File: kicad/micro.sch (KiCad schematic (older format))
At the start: 5 parts

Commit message: hardware prototype for v2.0 board
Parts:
- added P11: SERIAL, symbol CONN_3
- added R3: 1k, ~, symbol R
- added SW2: MODE SW, ~, symbol SWITCH_INV
- gave numbers to parts that had none: 5
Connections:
- net +5V: now also R3.1
- net GND: now also P11.3 (P3), SW2.1
- net RX: now reaches IC1.2 ((PCINT8/RXD0)PE0)
- net RX: now also P11.1 (P1)
- net TX: now reaches IC1.3 ((TXD0)PE1)
- net TX: now also P11.2 (PM)
- net A_FCMD_I: now reaches IC1.7 ((OC3C/INT5)PE5)
- net MODE: now reaches IC1.8 ((T3/INT6)PE6)
- net MODE: now also R3.2, SW2.2
- net A_ETHINT: no longer names the net of IC1.5 ((OC3A/AIN1)PE3)
- net A_FDCINT renamed A_FCFG_I
- net C_~RESET renamed ~RESET
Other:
- moved on the sheet: C11, C12, R1, X1
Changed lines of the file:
@@
 $Descr USLegal 14000 8500
 encoding utf-8
-Sheet 3 4
+Sheet 3 3
 Title "Color Computer FDC Ethernet Controller"
-Date "31 jul 2013"
+Date "4 aug 2013"
 Rev "2.0"
 Comp "Bexkat Systems LLC 2013"
@@
 $EndDescr
 $Comp
-L ATMEGA2560-A IC?
+L ATMEGA2560-A IC1
 U 1 1 51D5E753
 P 6550 4200
-F 0 "IC?" H 5400 7000 40  0000 L BNN
+F 0 "IC1" H 5400 7000 40  0000 L BNN
 F 1 "ATMEGA2560-A" H 7250 1350 40  0000 L BNN
 F 2 "TQFP100" H 6550 4200 30  0000 C CIN
@@
 Text HLabel 5050 6300 0    60   Output ~ 0
 A_~SELECT
-Text HLabel 5000 1600 0    60   Input ~ 0
-C_~RESET
-Text HLabel 8100 5500 2    60   Input ~ 0
-A_ETHINT
+Text HLabel 5250 1600 0    60   Input ~ 0
+~RESET
 Text HLabel 8100 5600 2    60   Input ~ 0
-A_FDCINT
-$Comp
-L +5V #PWR?
+A_FCFG_I
+$Comp
+L +5V #PWR043
 U 1 1 51D60C51
 P 6500 1200
-F 0 "#PWR?" H 6500 1290 20  0001 C CNN
+F 0 "#PWR043" H 6500 1290 20  0001 C CNN
 F 1 "+5V" H 6500 1290 30  0000 C CNN
 F 2 "" H 6500 1200 60  0000 C CNN
@@
 Connection ~ 6500 1300
 $Comp
-L GND #PWR?
+L GND #PWR044
 U 1 1 51D60C7D
 P 6550 7200
-F 0 "#PWR?" H 6550 7200 30  0001 C CNN
+F 0 "#PWR044" H 6550 7200 30  0001 C CNN
 F 1 "GND" H 6550 7130 30  0001 C CNN
 F 2 "" H 6550 7200 60  0000 C CNN
@@
 Connection ~ 6550 7100
 $Comp
-L CRYSTAL X?
+L CRYSTAL X1
 U 1 1 51D60CD1
-P 3550 2000
-F 0 "X?" H 3550 2150 60  0000 C CNN
-F 1 "16MHz" H 3550 1850 60  0000 C CNN
-F 2 "~" H 3550 2000 60  0000 C CNN
-F 3 "~" H 3550 2000 60  0000 C CNN
-	1    3550 2000
-	1    0    0    -1
-$EndComp
-$Comp
-L R R?
+P 1800 1400
+F 0 "X1" H 1800 1550 60  0000 C CNN
+F 1 "16MHz" H 1800 1250 60  0000 C CNN
+F 2 "~" H 1800 1400 60  0000 C CNN
+F 3 "~" H 1800 1400 60  0000 C CNN
+	1    1800 1400
+	1    0    0    -1
+$EndComp
+$Comp
+L R R1
 U 1 1 51D60CE0
-P 3550 1700
-F 0 "R?" V 3630 1700 40  0000 C CNN
-F 1 "1M" V 3557 1701 40  0000 C CNN
-F 2 "~" V 3480 1700 30  0000 C CNN
-F 3 "~" H 3550 1700 30  0000 C CNN
-	1    3550 1700
+P 1800 1100
+F 0 "R1" V 1880 1100 40  0000 C CNN
+F 1 "1M" V 1807 1101 40  0000 C CNN
+F 2 "~" V 1730 1100 30  0000 C CNN
+F 3 "~" H 1800 1100 30  0000 C CNN
+	1    1800 1100
 	0    -1   -1   0
 $EndComp
 $Comp
-L C C?
+L C C11
 U 1 1 51D60D15
-P 3250 2300
-F 0 "C?" H 3250 2400 40  0000 L CNN
-F 1 "22pF" H 3256 2215 40  0000 L CNN
-F 2 "~" H 3288 2150 30  0000 C CNN
-F 3 "~" H 3250 2300 60  0000 C CNN
-	1    3250 2300
-	1    0    0    -1
-$EndComp
-$Comp
-L C C?
+P 1500 1700
+F 0 "C11" H 1500 1800 40  0000 L CNN
+F 1 "22pF" H 1506 1615 40  0000 L CNN
+F 2 "~" H 1538 1550 30  0000 C CNN
+F 3 "~" H 1500 1700 60  0000 C CNN
+	1    1500 1700
+	1    0    0    -1
+$EndComp
+$Comp
+L C C12
 U 1 1 51D60D24
-P 3850 2300
-F 0 "C?" H 3850 2400 40  0000 L CNN
-F 1 "22pF" H 3856 2215 40  0000 L CNN
-F 2 "~" H 3888 2150 30  0000 C CNN
-F 3 "~" H 3850 2300 60  0000 C CNN
-	1    3850 2300
-	1    0    0    -1
-$EndComp
-Connection ~ 3850 2000
-Connection ~ 3250 2000
-Wire Wire Line
-	3250 2500 3850 2500
-$Comp
-L GND #PWR?
+P 2100 1700
+F 0 "C12" H 2100 1800 40  0000 L CNN
+F 1 "22pF" H 2106 1615 40  0000 L CNN
+F 2 "~" H 2138 1550 30  0000 C CNN
+F 3 "~" H 2100 1700 60  0000 C CNN
+	1    2100 1700
+	1    0    0    -1
+$EndComp
+Connection ~ 2100 1400
+Connection ~ 1500 1400
+Wire Wire Line
+	1500 1900 2100 1900
+$Comp
+L GND #PWR045
 U 1 1 51D60D76
-P 3550 2550
-F 0 "#PWR?" H 3550 2550 30  0001 C CNN
-F 1 "GND" H 3550 2480 30  0001 C CNN
-F 2 "" H 3550 2550 60  0000 C CNN
-F 3 "" H 3550 2550 60  0000 C CNN
-	1    3550 2550
-	1    0    0    -1
-$EndComp
-Wire Wire Line
-	3550 2500 3550 2550
-Connection ~ 3550 2500
-Wire Wire Line
-	3800 1700 3850 1700
-Wire Wire Line
-	3850 1700 3850 2100
-Wire Wire Line
-	3250 2100 3250 1700
-Wire Wire Line
-	3250 1700 3300 1700
-Text Label 3850 2000 0    60   ~ 0
+P 1800 1950
+F 0 "#PWR045" H 1800 1950 30  0001 C CNN
+F 1 "GND" H 1800 1880 30  0001 C CNN
+F 2 "" H 1800 1950 60  0000 C CNN
+F 3 "" H 1800 1950 60  0000 C CNN
+	1    1800 1950
+	1    0    0    -1
+$EndComp
+Wire Wire Line
+	1800 1900 1800 1950
+Connection ~ 1800 1900
+Wire Wire Line
+	2050 1100 2100 1100
+Wire Wire Line
+	2100 1100 2100 1500
+Wire Wire Line
+	1500 1500 1500 1100
+Wire Wire Line
+	1500 1100 1550 1100
+Text Label 2100 1400 0    60   ~ 0
 XTAL2
-Text Label 3250 2000 2    60   ~ 0
+Text Label 1500 1400 2    60   ~ 0
 XTAL1
 Text Label 5250 2200 2    60   ~ 0
@@
 	7850 2300 8050 2300
 Wire Wire Line
-	7850 5500 8100 5500
-Wire Wire Line
 	7850 5600 8100 5600
 Wire Wire Line
@@
 Wire Wire Line
 	5000 3200 5250 3200
-Wire Wire Line
-	5000 1600 5250 1600
+$Comp
+L CONN_3 P11
+U 1 1 51FB918E
+P 9350 5300
+F 0 "P11" V 9300 5300 50  0000 C CNN
+F 1 "SERIAL" V 9400 5300 40  0000 C CNN
+F 2 "" H 9350 5300 60  0000 C CNN
+F 3 "" H 9350 5300 60  0000 C CNN
+	1    9350 5300
+	1    0    0    -1
+$EndComp
+Wire Wire Line
+	7850 5200 9000 5200
+Wire Wire Line
+	7850 5300 9000 5300
+$Comp
+L GND #PWR046
+U 1 1 51FB9229
+P 8950 5500
+F 0 "#PWR046" H 8950 5500 30  0001 C CNN
+F 1 "GND" H 8950 5430 30  0001 C CNN
+F 2 "" H 8950 5500 60  0000 C CNN
+F 3 "" H 8950 5500 60  0000 C CNN
+	1    8950 5500
+	1    0    0    -1
+$EndComp
+Wire Wire Line
+	8950 5500 8950 5400
+Wire Wire Line
+	8950 5400 9000 5400
+$Comp
+L SWITCH_INV SW2
+U 1 1 51FC2D05
+P 10500 5800
+F 0 "SW2" H 10300 5950 50  0000 C CNN
+F 1 "MODE SW" H 10350 5650 50  0000 C CNN
+F 2 "~" H 10500 5800 60  0000 C CNN
+F 3 "~" H 10500 5800 60  0000 C CNN
+	1    10500 5800
+	1    0    0    -1
+$EndComp
+Text HLabel 8100 5700 2    60   Input ~ 0
+A_FCMD_I
+Wire Wire Line
+	7850 5700 8100 5700
+$Comp
+L +5V #PWR047
+U 1 1 51FC56B4
+P 9750 5200
+F 0 "#PWR047" H 9750 5290 20  0001 C CNN
+F 1 "+5V" H 9750 5290 30  0000 C CNN
+F 2 "" H 9750 5200 60  0000 C CNN
+F 3 "" H 9750 5200 60  0000 C CNN
+	1    9750 5200
+	1    0    0    -1
+$EndComp
+$Comp
+L R R3
+U 1 1 51FC56DA
+P 9750 5550
+F 0 "R3" V 9830 5550 40  0000 C CNN
+F 1 "1k" V 9757 5551 40  0000 C CNN
+F 2 "~" V 9680 5550 30  0000 C CNN
+F 3 "~" H 9750 5550 30  0000 C CNN
+	1    9750 5550
+	1    0    0    -1
+$EndComp
+Wire Wire Line
+	9750 5200 9750 5300
+Wire Wire Line
+	7850 5800 10000 5800
+Connection ~ 9750 5800
+$Comp
+L GND #PWR048
+U 1 1 51FC57B8
+P 11100 6000
+F 0 "#PWR048" H 11100 6000 30  0001 C CNN
+F 1 "GND" H 11100 5930 30  0001 C CNN
+F 2 "" H 11100 6000 60  0000 C CNN
+F 3 "" H 11100 6000 60  0000 C CNN
+	1    11100 6000
+	1    0    0    -1
+$EndComp
+Text Label 8850 5800 0    60   ~ 0
+MODE
+Text Label 7850 5200 0    60   ~ 0
+RX
+Text Label 7850 5300 0    60   ~ 0
+TX
+Wire Wire Line
+	11000 5700 11100 5700
+Wire Wire Line
+	11100 5700 11100 6000
 $EndSCHEMATC

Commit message: start of additional goodness and fixes
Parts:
- removed R3: 1k, ~, symbol R
- added D10: A0, symbol LED
- added D11: A1, symbol LED
- added D12: A2, symbol LED
- added D13: A3, symbol LED
- added RP2: 150, symbol R_PACK4
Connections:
- net GND: now also D10.2 (K), D11.2 (K), D12.2 (K), D13.2 (K)
- net LED0: now reaches IC1.15 (PH3(OC4A))
- net LED0: now also RP2.1 (P1)
- net LED1: now reaches IC1.16 (PH4(OC4B))
- net LED1: now also RP2.2 (P2)
- net LED2: now reaches IC1.17 (PH5(OC4C))
- net LED2: now also RP2.3 (P3)
- net LED3: now reaches IC1.18 (PH6(OC2B))
- net LED3: now also RP2.4 (P4)
- new net: D13.1 (A), RP2.5 (R4)
- new net: D11.1 (A), RP2.7 (R2)
- new net: D10.1 (A), RP2.8 (R1)
- new net: D12.1 (A), RP2.6 (R3)
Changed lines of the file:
@@
 Sheet 3 3
 Title "Color Computer FDC Ethernet Controller"
-Date "4 aug 2013"
-Rev "2.0"
+Date "20 aug 2013"
+Rev "2.1"
 Comp "Bexkat Systems LLC 2013"
 Comment1 ""
@@
 A_FCFG_I
 $Comp
-L +5V #PWR043
+L +5V #PWR47
 U 1 1 51D60C51
 P 6500 1200
-F 0 "#PWR043" H 6500 1290 20  0001 C CNN
+F 0 "#PWR47" H 6500 1290 20  0001 C CNN
 F 1 "+5V" H 6500 1290 30  0000 C CNN
 F 2 "" H 6500 1200 60  0000 C CNN
@@
 Connection ~ 6500 1300
 $Comp
-L GND #PWR044
+L GND #PWR48
 U 1 1 51D60C7D
 P 6550 7200
-F 0 "#PWR044" H 6550 7200 30  0001 C CNN
+F 0 "#PWR48" H 6550 7200 30  0001 C CNN
 F 1 "GND" H 6550 7130 30  0001 C CNN
 F 2 "" H 6550 7200 60  0000 C CNN
@@
 	1500 1900 2100 1900
 $Comp
-L GND #PWR045
+L GND #PWR45
 U 1 1 51D60D76
 P 1800 1950
-F 0 "#PWR045" H 1800 1950 30  0001 C CNN
+F 0 "#PWR45" H 1800 1950 30  0001 C CNN
 F 1 "GND" H 1800 1880 30  0001 C CNN
 F 2 "" H 1800 1950 60  0000 C CNN
@@
 	7850 5300 9000 5300
 $Comp
-L GND #PWR046
+L GND #PWR49
 U 1 1 51FB9229
 P 8950 5500
-F 0 "#PWR046" H 8950 5500 30  0001 C CNN
+F 0 "#PWR49" H 8950 5500 30  0001 C CNN
 F 1 "GND" H 8950 5430 30  0001 C CNN
 F 2 "" H 8950 5500 60  0000 C CNN
@@
 Wire Wire Line
 	7850 5700 8100 5700
-$Comp
-L +5V #PWR047
-U 1 1 51FC56B4
-P 9750 5200
-F 0 "#PWR047" H 9750 5290 20  0001 C CNN
-F 1 "+5V" H 9750 5290 30  0000 C CNN
-F 2 "" H 9750 5200 60  0000 C CNN
-F 3 "" H 9750 5200 60  0000 C CNN
-	1    9750 5200
-	1    0    0    -1
-$EndComp
-$Comp
-L R R3
-U 1 1 51FC56DA
-P 9750 5550
-F 0 "R3" V 9830 5550 40  0000 C CNN
-F 1 "1k" V 9757 5551 40  0000 C CNN
-F 2 "~" V 9680 5550 30  0000 C CNN
-F 3 "~" H 9750 5550 30  0000 C CNN
-	1    9750 5550
-	1    0    0    -1
-$EndComp
-Wire Wire Line
-	9750 5200 9750 5300
 Wire Wire Line
 	7850 5800 10000 5800
-Connection ~ 9750 5800
-$Comp
-L GND #PWR048
+$Comp
+L GND #PWR50
 U 1 1 51FC57B8
 P 11100 6000
-F 0 "#PWR048" H 11100 6000 30  0001 C CNN
+F 0 "#PWR50" H 11100 6000 30  0001 C CNN
 F 1 "GND" H 11100 5930 30  0001 C CNN
 F 2 "" H 11100 6000 60  0000 C CNN
@@
 Wire Wire Line
 	11100 5700 11100 6000
+Wire Wire Line
+	2550 4400 2400 4400
+Wire Wire Line
+	2400 4400 2400 4000
+Wire Wire Line
+	2400 4000 2200 4000
+Connection ~ 1800 4700
+Connection ~ 1800 4350
+Wire Wire Line
+	1800 4000 1800 5150
+Wire Wire Line
+	2550 4500 2300 4500
+Wire Wire Line
+	2300 4500 2300 4350
+Wire Wire Line
+	2300 4350 2200 4350
+Text Label 2950 4700 0    60   ~ 0
+LED3
+$Comp
+L LED D11
+U 1 1 5213E542
+P 2000 4350
+F 0 "D11" H 2000 4450 50  0000 C CNN
+F 1 "A1" H 2000 4250 50  0000 C CNN
+F 2 "" H 2000 4350 60  0001 C CNN
+F 3 "" H 2000 4350 60  0001 C CNN
+	1    2000 4350
+	-1   0    0    1
+$EndComp
+$Comp
+L GND #PWR46
+U 1 1 5213E548
+P 1800 5150
+F 0 "#PWR46" H 1800 5150 30  0001 C CNN
+F 1 "GND" H 1800 5080 30  0001 C CNN
+F 2 "" H 1800 5150 60  0001 C CNN
+F 3 "" H 1800 5150 60  0001 C CNN
+	1    1800 5150
+	1    0    0    -1
+$EndComp
+$Comp
+L LED D10
+U 1 1 5213E54E
+P 2000 4000
+F 0 "D10" H 2000 4100 50  0000 C CNN
+F 1 "A0" H 2000 3900 50  0000 C CNN
+F 2 "" H 2000 4000 60  0001 C CNN
+F 3 "" H 2000 4000 60  0001 C CNN
+	1    2000 4000
+	-1   0    0    1
+$EndComp
+Text Label 2950 4500 0    60   ~ 0
+LED1
+Text Label 2950 4600 0    60   ~ 0
+LED2
+Text Label 2950 4400 0    60   ~ 0
+LED0
+Text Label 5250 5500 2    60   ~ 0
+LED0
+Text Label 5250 5600 2    60   ~ 0
+LED1
+Text Label 5250 5700 2    60   ~ 0
+LED2
+Text Label 5250 5800 2    60   ~ 0
+LED3
+Connection ~ 1800 5000
+Wire Wire Line
+	2300 4700 2200 4700
+Wire Wire Line
+	2300 4600 2300 4700
+Wire Wire Line
+	2550 4600 2300 4600
+Wire Wire Line
+	2400 4700 2550 4700
+Wire Wire Line
+	2400 5000 2400 4700
+Wire Wire Line
+	2200 5000 2400 5000
+$Comp
+L LED D12
+U 1 1 5213E554
+P 2000 4700
+F 0 "D12" H 2000 4800 50  0000 C CNN
+F 1 "A2" H 2000 4600 50  0000 C CNN
+F 2 "" H 2000 4700 60  0001 C CNN
+F 3 "" H 2000 4700 60  0001 C CNN
+	1    2000 4700
+	-1   0    0    1
+$EndComp
+$Comp
+L LED D13
+U 1 1 5213E53C
+P 2000 5000
+F 0 "D13" H 2000 5100 50  0000 C CNN
+F 1 "A3" H 2000 4900 50  0000 C CNN
+F 2 "" H 2000 5000 60  0001 C CNN
+F 3 "" H 2000 5000 60  0001 C CNN
+	1    2000 5000
+	-1   0    0    1
+$EndComp
+$Comp
+L R_PACK4 RP2
+U 1 1 5213E55D
+P 2750 4750
+F 0 "RP2" H 2750 5200 40  0000 C CNN
+F 1 "150" H 2750 4700 40  0000 C CNN
+F 2 "" H 2750 4750 60  0001 C CNN
+F 3 "" H 2750 4750 60  0001 C CNN
+	1    2750 4750
+	-1   0    0    -1
+$EndComp
 $EndSCHEMATC

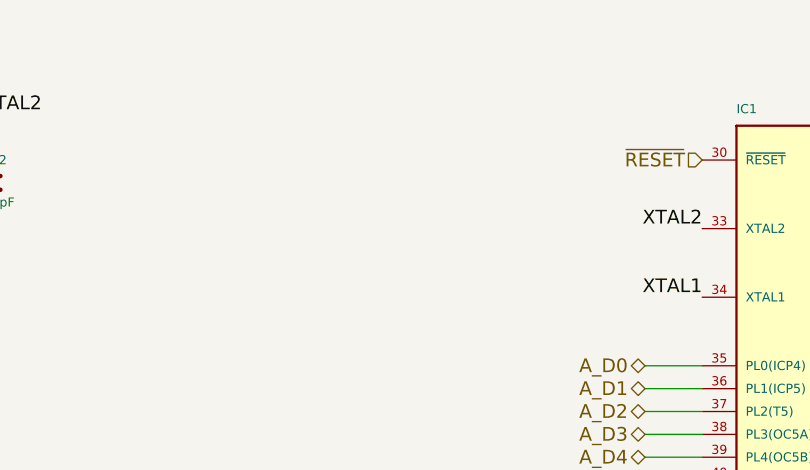
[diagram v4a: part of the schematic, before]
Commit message: first draft of v2.1 hardware.  Added some addition diagnostic leds, power indicators, and a separate SPI interface for the 5v side.  Maybe add support for external LCD?
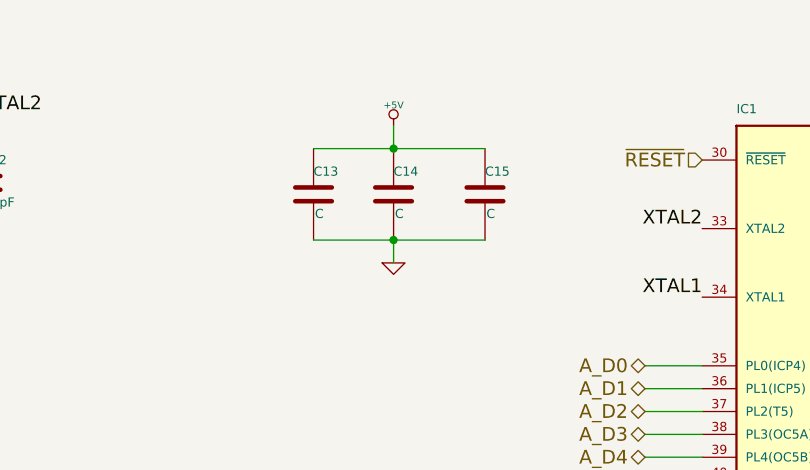
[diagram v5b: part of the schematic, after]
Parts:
- added C13, C14, C15: C, ~, symbol C
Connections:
- net +5V: now also C13.1, C14.1, C15.1
- net GND: now also C13.2, C14.2, C15.2
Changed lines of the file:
@@
 Sheet 3 3
 Title "Color Computer FDC Ethernet Controller"
-Date "21 aug 2013"
+Date "25 aug 2013"
 Rev "2.1"
 Comp "Bexkat Systems LLC 2013"
@@
 A_FCFG_I
 $Comp
-L +5V #PWR47
+L +5V #PWR045
 U 1 1 51D60C51
 P 6500 1200
-F 0 "#PWR47" H 6500 1290 20  0001 C CNN
+F 0 "#PWR045" H 6500 1290 20  0001 C CNN
 F 1 "+5V" H 6500 1290 30  0000 C CNN
 F 2 "" H 6500 1200 60  0000 C CNN
@@
 Connection ~ 6500 1300
 $Comp
-L GND #PWR48
+L GND #PWR046
 U 1 1 51D60C7D
 P 6550 7200
-F 0 "#PWR48" H 6550 7200 30  0001 C CNN
+F 0 "#PWR046" H 6550 7200 30  0001 C CNN
 F 1 "GND" H 6550 7130 30  0001 C CNN
 F 2 "" H 6550 7200 60  0000 C CNN
@@
 	1500 1900 2100 1900
 $Comp
-L GND #PWR45
+L GND #PWR047
 U 1 1 51D60D76
 P 1800 1950
-F 0 "#PWR45" H 1800 1950 30  0001 C CNN
+F 0 "#PWR047" H 1800 1950 30  0001 C CNN
 F 1 "GND" H 1800 1880 30  0001 C CNN
 F 2 "" H 1800 1950 60  0000 C CNN
@@
 	7850 5300 9000 5300
 $Comp
-L GND #PWR49
+L GND #PWR048
 U 1 1 51FB9229
 P 8950 5500
-F 0 "#PWR49" H 8950 5500 30  0001 C CNN
+F 0 "#PWR048" H 8950 5500 30  0001 C CNN
 F 1 "GND" H 8950 5430 30  0001 C CNN
 F 2 "" H 8950 5500 60  0000 C CNN
@@
 	7850 5800 10000 5800
 $Comp
-L GND #PWR50
+L GND #PWR049
 U 1 1 51FC57B8
 P 11100 6000
-F 0 "#PWR50" H 11100 6000 30  0001 C CNN
+F 0 "#PWR049" H 11100 6000 30  0001 C CNN
 F 1 "GND" H 11100 5930 30  0001 C CNN
 F 2 "" H 11100 6000 60  0000 C CNN
@@
 $EndComp
 $Comp
-L GND #PWR46
+L GND #PWR050
 U 1 1 5213E548
 P 1800 5150
-F 0 "#PWR46" H 1800 5150 30  0001 C CNN
+F 0 "#PWR050" H 1800 5150 30  0001 C CNN
 F 1 "GND" H 1800 5080 30  0001 C CNN
 F 2 "" H 1800 5150 60  0001 C CNN
@@
 	-1   0    0    -1
 $EndComp
+$Comp
+L C C13
+U 1 1 52196D2B
+P 3550 1750
+F 0 "C13" H 3550 1850 40  0000 L CNN
+F 1 "C" H 3556 1665 40  0000 L CNN
+F 2 "~" H 3588 1600 30  0000 C CNN
+F 3 "~" H 3550 1750 60  0000 C CNN
+	1    3550 1750
+	1    0    0    -1
+$EndComp
+$Comp
+L C C14
+U 1 1 52196D3A
+P 3900 1750
+F 0 "C14" H 3900 1850 40  0000 L CNN
+F 1 "C" H 3906 1665 40  0000 L CNN
+F 2 "~" H 3938 1600 30  0000 C CNN
+F 3 "~" H 3900 1750 60  0000 C CNN
+	1    3900 1750
+	1    0    0    -1
+$EndComp
+$Comp
+L C C15
+U 1 1 52196D49
+P 4300 1750
+F 0 "C15" H 4300 1850 40  0000 L CNN
+F 1 "C" H 4306 1665 40  0000 L CNN
+F 2 "~" H 4338 1600 30  0000 C CNN
+F 3 "~" H 4300 1750 60  0000 C CNN
+	1    4300 1750
+	1    0    0    -1
+$EndComp
+$Comp
+L +5V #PWR051
+U 1 1 52196D56
+P 3900 1450
+F 0 "#PWR051" H 3900 1540 20  0001 C CNN
+F 1 "+5V" H 3900 1540 30  0000 C CNN
+F 2 "" H 3900 1450 60  0000 C CNN
+F 3 "" H 3900 1450 60  0000 C CNN
+	1    3900 1450
+	1    0    0    -1
+$EndComp
+$Comp
+L GND #PWR052
+U 1 1 52196D5C
+P 3900 2050
+F 0 "#PWR052" H 3900 2050 30  0001 C CNN
+F 1 "GND" H 3900 1980 30  0001 C CNN
+F 2 "" H 3900 2050 60  0000 C CNN
+F 3 "" H 3900 2050 60  0000 C CNN
+	1    3900 2050
+	1    0    0    -1
+$EndComp
+Wire Wire Line
+	3550 1950 4300 1950
+Wire Wire Line
+	3900 1950 3900 2050
+Connection ~ 3900 1950
+Wire Wire Line
+	3550 1550 4300 1550
+Connection ~ 3900 1550
+Wire Wire Line
+	3900 1550 3900 1450
 $EndSCHEMATC
